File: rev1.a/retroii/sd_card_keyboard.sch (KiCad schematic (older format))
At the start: 63 parts, among them CON1 SD_Card_SPI, J22 Conn_01x09, K1 PS2_KEYBOARD, P2 PROP_PLUG, Q5 2N3904, SW3 SAVE, SW4 LOAD, SW5 SW_PUSH_SAFE, SW6 RESET, SW7 MISC1, SW8 MISC2, U16 Prop_P8X32A, U17 24LC256_EEPROM, Y3 5MHz 20pf

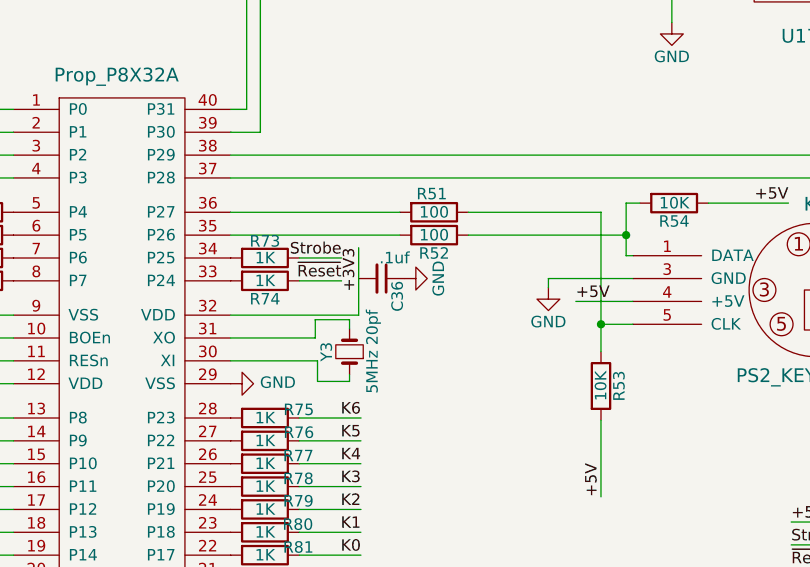
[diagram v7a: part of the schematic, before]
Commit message: routing audio and keyboard/sd interface
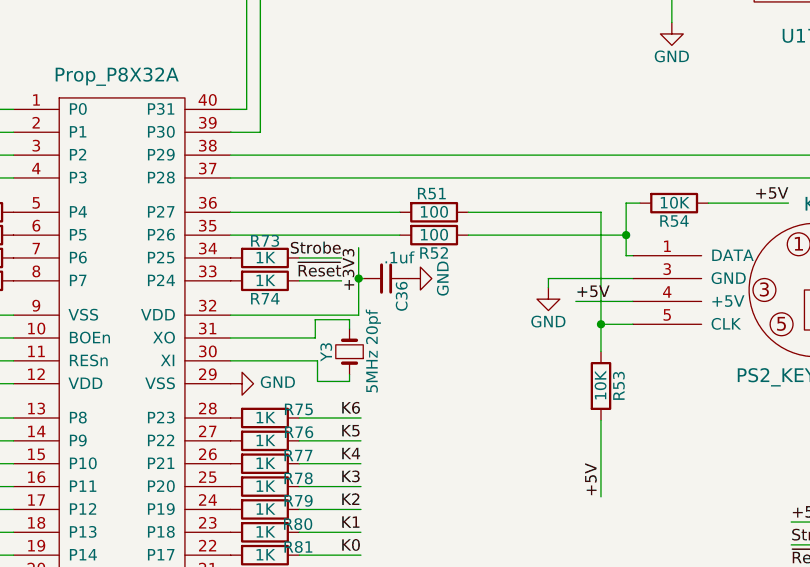
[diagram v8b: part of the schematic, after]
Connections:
- net +3V3: now also C36.2
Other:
- moved on the sheet: C36
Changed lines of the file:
@@
 L power1:GND #PWR071
 U 1 1 56E3AD99
-P 5740 3250
-F 0 "#PWR071" H 5740 3000 50  0001 C CNN
-F 1 "GND" H 5740 3100 50  0000 C CNN
-F 2 "" H 5740 3250 60  0000 C CNN
-F 3 "" H 5740 3250 60  0000 C CNN
-	1    5740 3250
+P 5760 3250
+F 0 "#PWR071" H 5760 3000 50  0001 C CNN
+F 1 "GND" H 5760 3100 50  0000 C CNN
+F 2 "" H 5760 3250 60  0000 C CNN
+F 3 "" H 5760 3250 60  0000 C CNN
+	1    5760 3250
 	0    -1   -1   0
 $EndComp
@@
 L device:C_Small C36
 U 1 1 56E3ADD9
-P 5640 3250
-F 0 "C36" H 5650 3320 50  0000 L CNN
-F 1 ".1uf" V 5550 3240 50  0000 L CNN
-F 2 "retroii_footprints:C_Disc_D3.0mm_W2.0mm_P2.50mm" H 5640 3250 60  0001 C CNN
-F 3 "" H 5640 3250 60  0000 C CNN
-	1    5640 3250
+P 5660 3250
+F 0 "C36" H 5670 3320 50  0000 L CNN
+F 1 ".1uf" V 5570 3240 50  0000 L CNN
+F 2 "retroii_footprints:C_Disc_D3.0mm_W2.0mm_P2.50mm" H 5660 3250 60  0001 C CNN
+F 3 "" H 5660 3250 60  0000 C CNN
+	1    5660 3250
 	0    1    1    0
 $EndComp
@@
 	3710 4260 4030 4260
 Wire Wire Line
-	5540 3115 5540 3410
+	5540 3115 5540 3250
 Wire Wire Line
 	5280 3160 5465 3160
@@
 Wire Wire Line
 	5035 4705 4005 4705
+Wire Wire Line
+	5560 3250 5540 3250
 Wire Bus Line
 	10725 2260 10725 5405
+Connection ~ 5540 3250
+Wire Wire Line
+	5540 3250 5540 3410
 $EndSCHEMATC
